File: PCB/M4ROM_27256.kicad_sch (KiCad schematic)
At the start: 7 parts, among them J1 32Kx8_mask_rom_socket, J2 4ROM_prog_female, SW1 CUS-14TB, U1 29F010

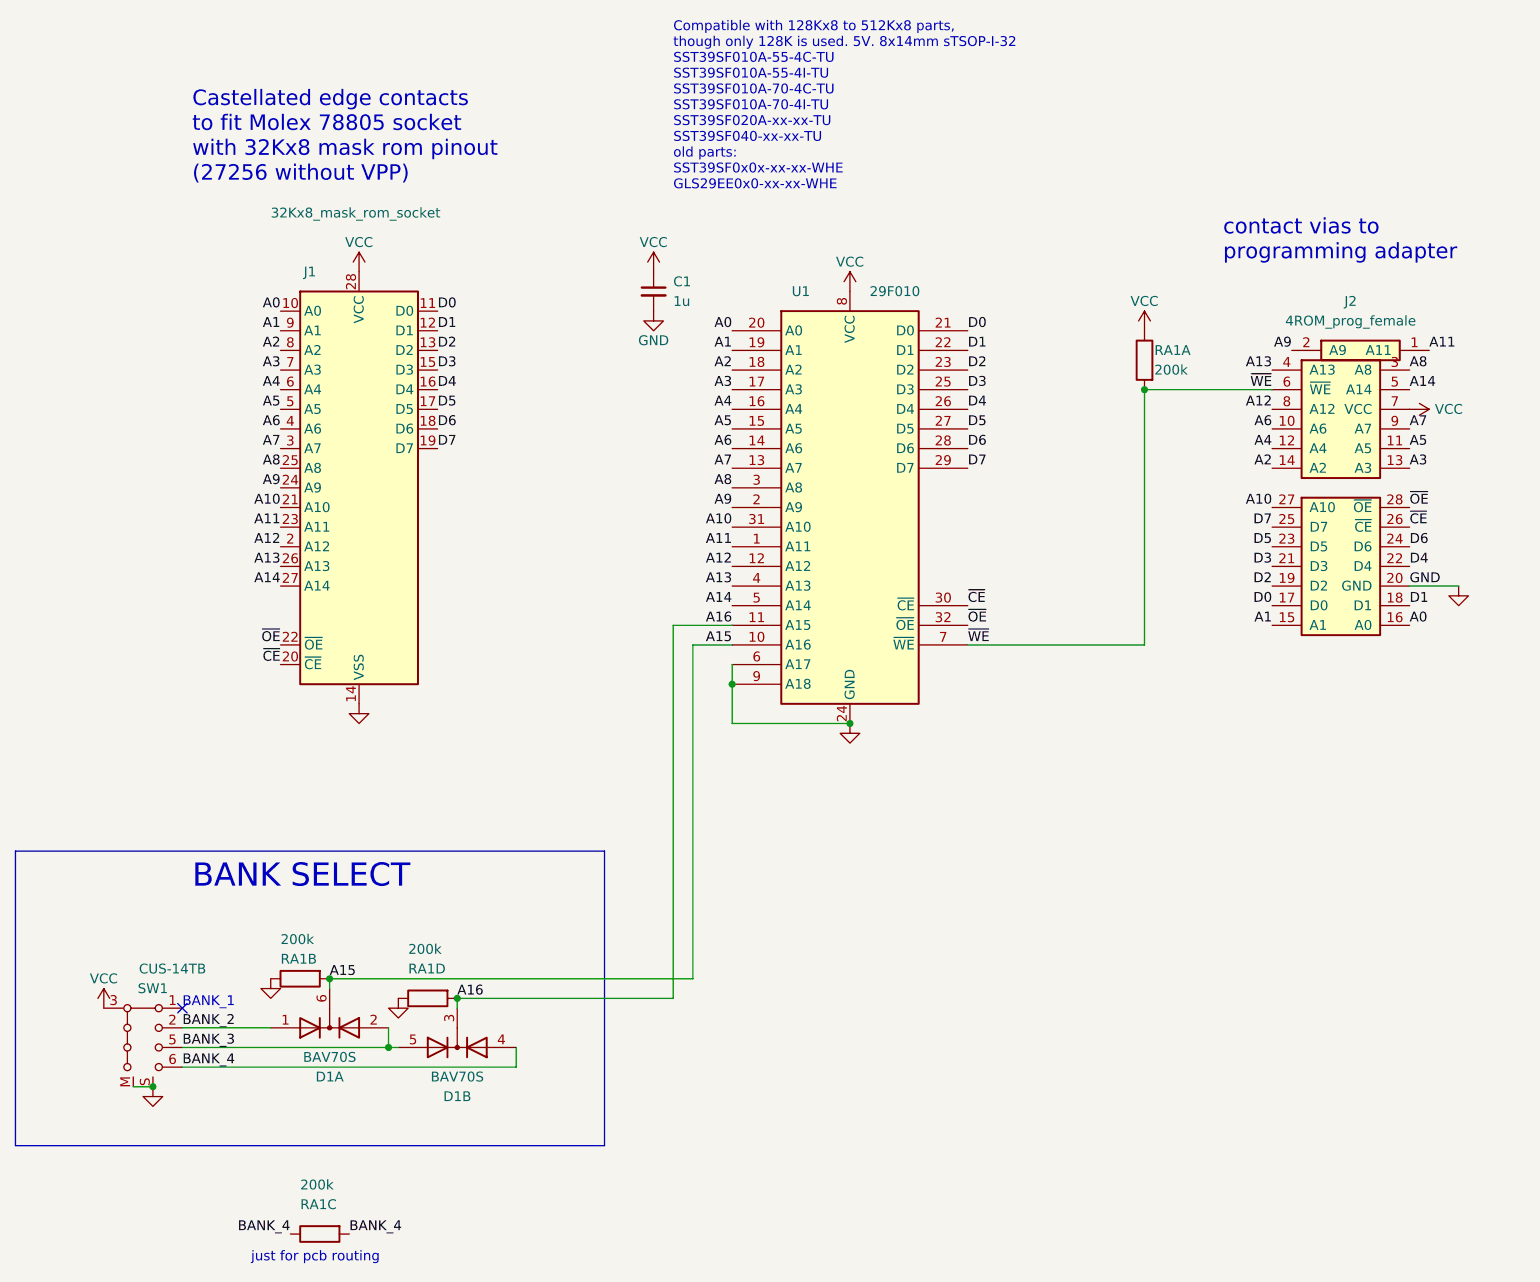
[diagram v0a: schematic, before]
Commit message: simpler diodes
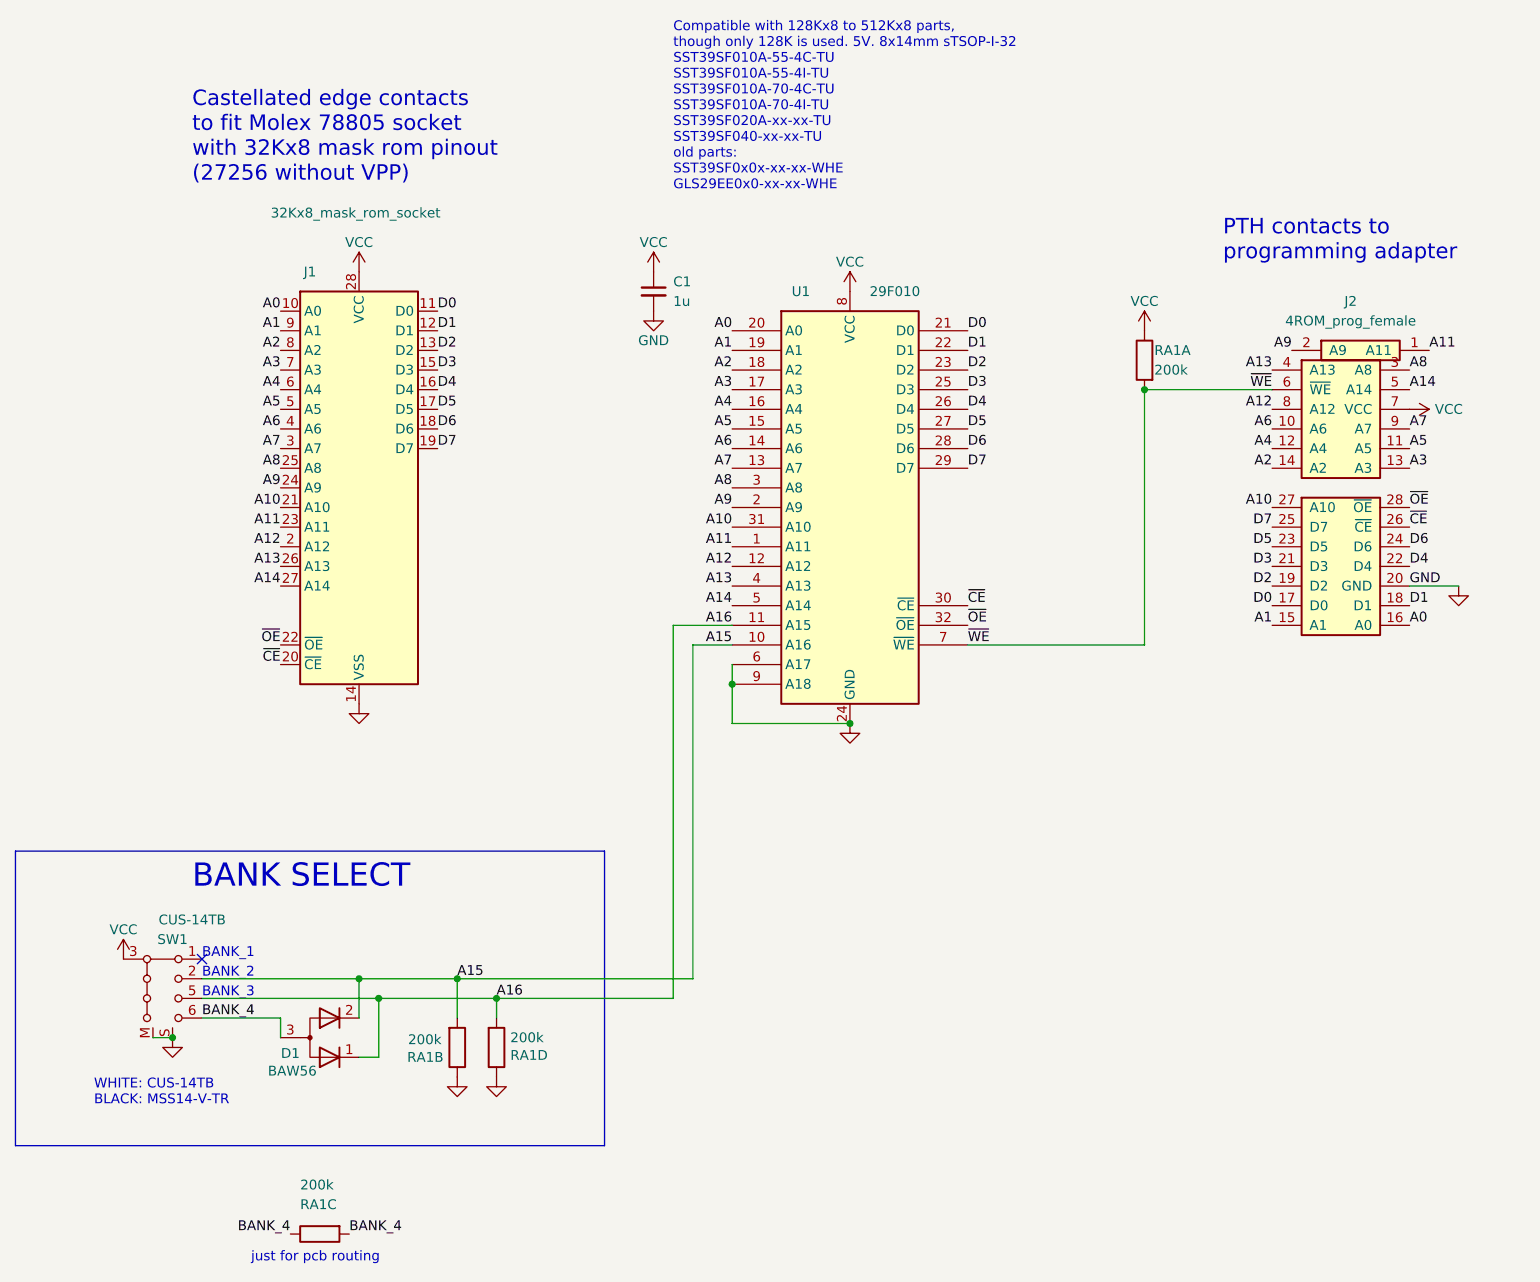
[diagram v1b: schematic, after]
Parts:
- removed D1: BAV70S, 000_LOCAL:TSSOP-6-symmetric, symbol 000_LOCAL:BAV70S
- added D1: BAW56, 000_LOCAL:SOT-23, symbol 000_LOCAL:D_Dual_CommonAnode_KKA_Parallel
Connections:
- net BANK_2 is gone; now on net A15: SW1.2
- net BANK_3 is gone; now on net A16: SW1.5
- net A15: now also D1.2 (K)
- net A16: now also D1.1 (K)
- net BANK_4: now also D1.3 (A)
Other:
- note added: "BANK_2"
- note added: "BANK_3"
- note added: "PTH contacts to programming adapter"
- note added: "WHITE: CUS-14TB BLACK: MSS14-V-TR"
- note removed: "contact vias to programming adapter"
- moved on the sheet: RA1B, RA1D, SW1
